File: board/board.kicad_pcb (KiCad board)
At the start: 4 copper layers, 21 x 61 mm, 44 parts, among them J1 UART, J2 008_USB, J3 DebugEdge_02x05, J4 SPI_2x3, J5 ADC_2x3, J6 I2C_2x2, J7 SPI_2x3, J8 I2C_2x2, J9 UART_2x2, U1 W25Q128JVS, U2 RP2040, Y1 12MhZ

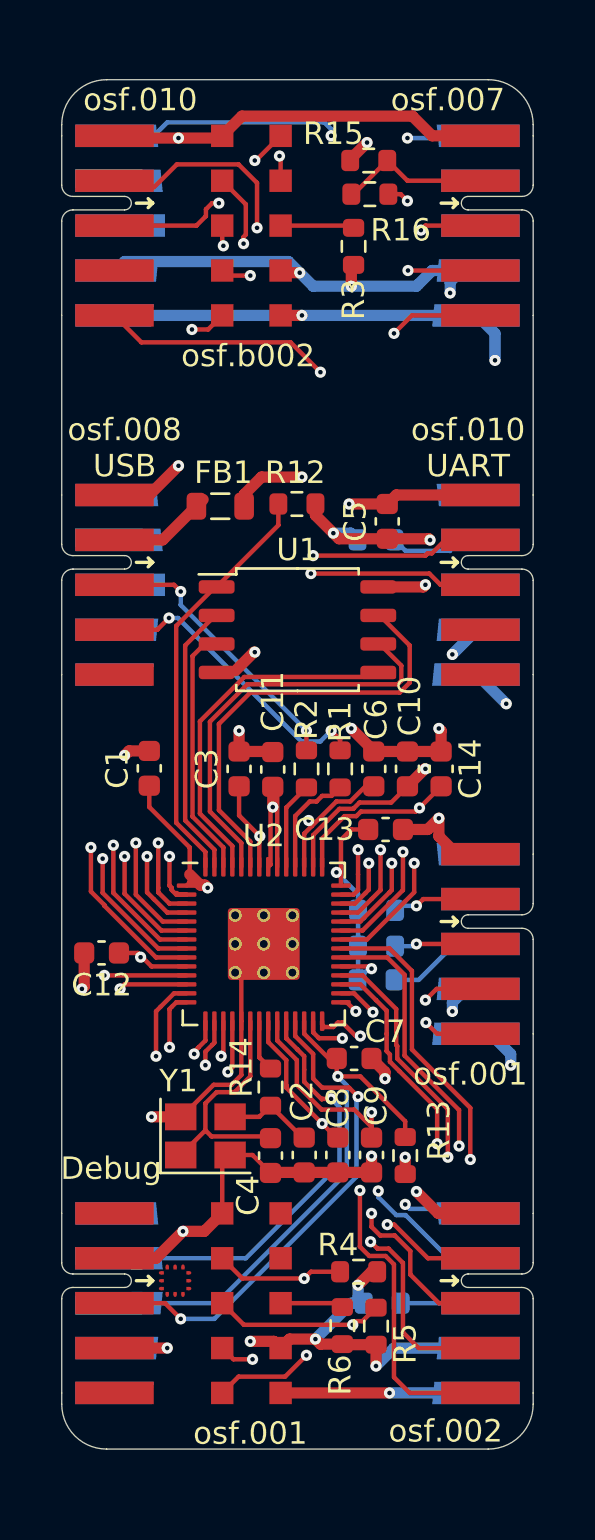
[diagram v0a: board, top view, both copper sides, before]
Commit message: changed top I2C connector to be a UNIO connector for a mac address chip
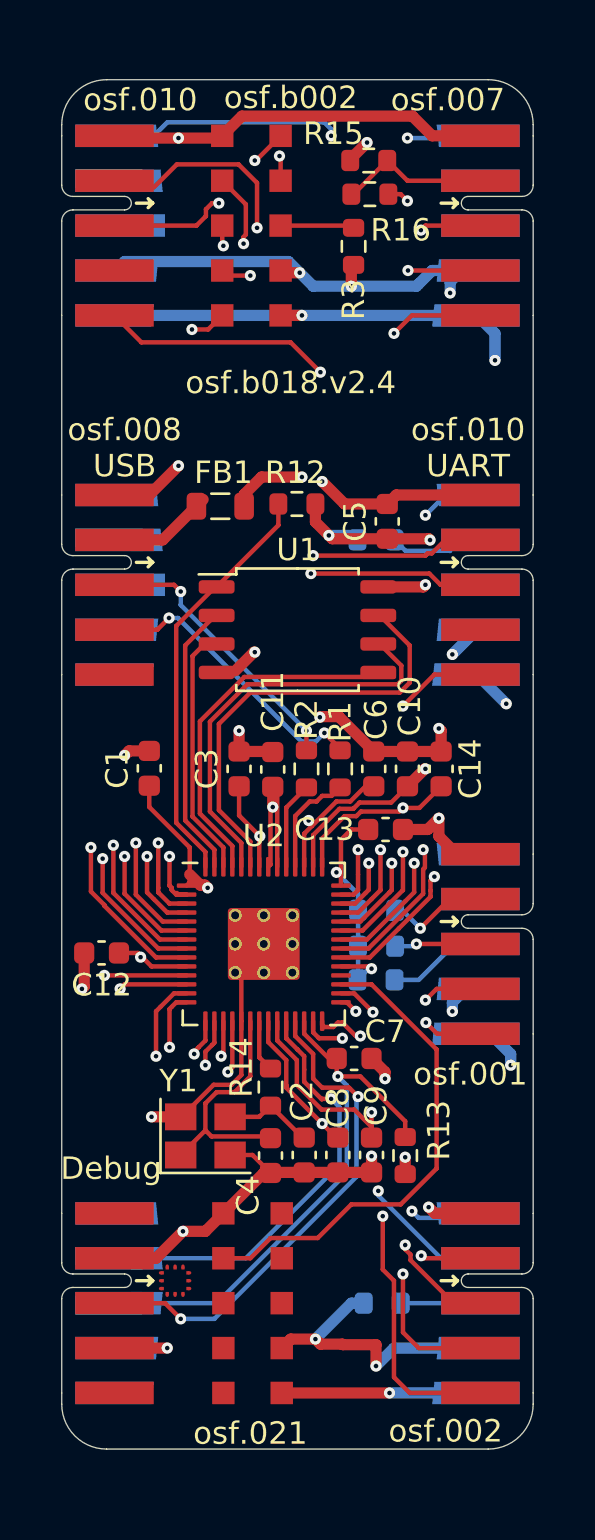
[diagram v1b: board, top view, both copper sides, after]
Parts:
- removed R4, R5: 2k, Resistor_SMD:R_0603_1608Metric
- removed R6: 10k, Resistor_SMD:R_0603_1608Metric
- J6: value I2C_2x2 -> 021_single_IO_UNIO
- moved J6 0.05 mm to (150.8, 96.5)
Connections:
- net /I2C0_SDA renamed /rp2040/GPIO20
- J6 pad 3: /I2C0_SCL -> (no net)
- J6 pad 4: /GPIO23 -> (no net)
- J6 pad 5: /GPIO22 -> (no net)
- J6 pad 8: Net-(J6-Pad8) -> (no net)
- J9 pad 5: unconnected-(J9-Pad5) -> /GPIO23
- J9 pad 6: unconnected-(J9-Pad6) -> /GPIO22
- U2 pad 32: /I2C0_SCL -> /rp2040/GPIO21
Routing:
- net /I2C0_SCL: track 27.4 -> 0.00 mm, vias 2 -> 0
- net /GPIO23: track 30.2 -> 17.8 mm
- net /GPIO22: track 29.2 -> 25.7 mm
- net +3V3: track 199.4 -> 196.4 mm, vias 22 -> 20
- net /rp2040/GPIO20: track 24.7 -> 21.9 mm, vias 2 -> 0
- net Net-(J6-Pad8): track 2.82 -> 0.00 mm
- net GND: track 166.7 -> 167.7 mm
- net /GPIO24: track 42.8 -> 41.9 mm
- net /GPIO25: track 52.5 -> 51.6 mm
- net /~{SPI1_CS}: track 17.4 -> 18.2 mm
- net /SPI1_RX: track 20.7 -> 20.0 mm
- net Net-(C14-Pad1): track 36.8 -> 37.4 mm
- net /GPIO14: track 24.6 -> 24.1 mm
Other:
- board text added: "osf.021"
- board text added: "osf.b018.v2.4"

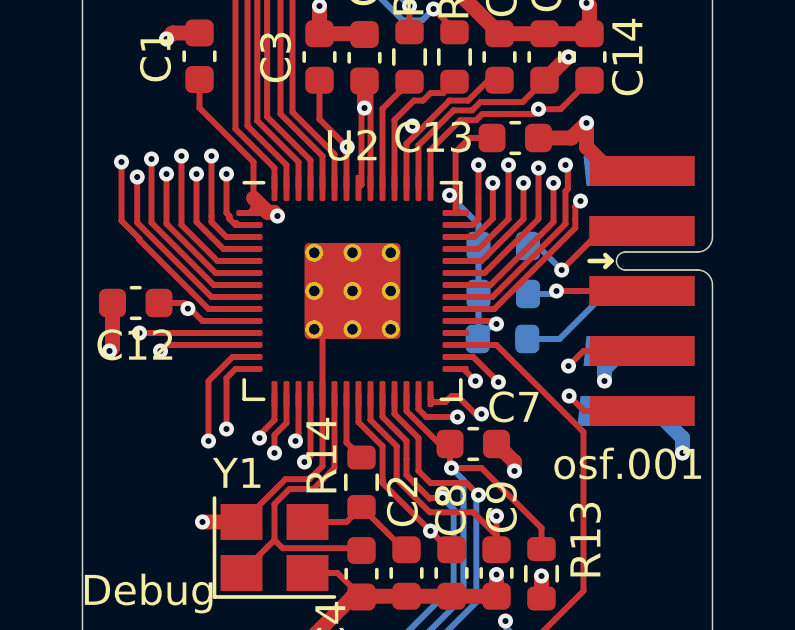
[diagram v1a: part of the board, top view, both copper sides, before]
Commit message: changed power symbols in subsheets
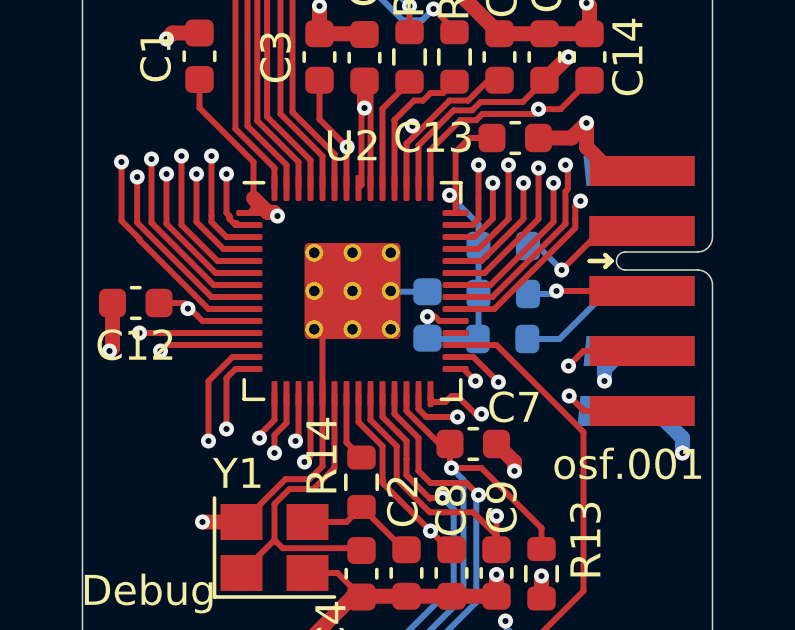
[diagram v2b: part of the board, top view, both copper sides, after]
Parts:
- added C29: 100nF, Capacitor_SMD:C_0603_1608Metric, B.Cu at (151.5, 81.3)
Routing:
- net GND: track 167.7 -> 169.0 mm
- net +3V3: track 196.4 -> 197.6 mm
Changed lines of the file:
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@@
       ) (layer "B.SilkS") (width 0.01) (fill solid))
+  )
+  (footprint "Capacitor_SMD:C_0603_1608Metric" (layer "B.Cu")
+    (at 151.5 81.3 90)
+    (descr "Capacitor SMD 0603 (1608 Metric), square (rectangular) end terminal, IPC_7351 nominal, (Body size source: IPC-SM-782 page 76, https://www.pcb-3d.com/wordpress/wp-content/uploads/ipc-sm-782a_amendment_1_and_2.pdf), generated with kicad-footprint-generator")
+    (tags "capacitor")
+    (property "Sheetfile" "rp2040.kicad_sch")
+    (property "Sheetname" "rp2040")
+    (attr smd)
+    (fp_text reference "C29" (at 0 1.43 90) (layer "B.SilkS")
+      (effects (font (size 1 1) (thickness 0.15)) (justify mirror))
+    )
+    (fp_text value "100nF" (at 0 -1.43 90) (layer "B.Fab")
+      (effects (font (size 1 1) (thickness 0.15)) (justify mirror))
+    )
+    (fp_text user "${REFERENCE}" (at 0 0 90) (layer "B.Fab")
+      (effects (font (size 0.4 0.4) (thickness 0.06)) (justify mirror))
+    )
+    (fp_line (start -0.14058 0.51) (end 0.14058 0.51) (layer "B.SilkS") (width 0.12))
+    (fp_line (start -0.14058 -0.51) (end 0.14058 -0.51) (layer "B.SilkS") (width 0.12))
+    (fp_line (start -1.48 -0.73) (end -1.48 0.73) (layer "B.CrtYd") (width 0.05))
+    (fp_line (start -1.48 0.73) (end 1.48 0.73) (layer "B.CrtYd") (width 0.05))
+    (fp_line (start 1.48 -0.73) (end -1.48 -0.73) (layer "B.CrtYd") (width 0.05))
+    (fp_line (start 1.48 0.73) (end 1.48 -0.73) (layer "B.CrtYd") (width 0.05))
+    (fp_line (start 0.8 0.4) (end 0.8 -0.4) (layer "B.Fab") (width 0.1))
+    (fp_line (start -0.8 0.4) (end 0.8 0.4) (layer "B.Fab") (width 0.1))
+    (fp_line (start -0.8 -0.4) (end -0.8 0.4) (layer "B.Fab") (width 0.1))
+    (fp_line (start 0.8 -0.4) (end -0.8 -0.4) (layer "B.Fab") (width 0.1))
+    (pad "1" smd roundrect (at -0.775 0 90) (size 0.9 0.95) (layers "B.Cu" "B.Paste" "B.Mask") (roundrect_rratio 0.25)
+      (net 1 "+3V3") (pintype "passive"))
+    (pad "2" smd roundrect (at 0.775 0 90) (size 0.9 0.95) (layers "B.Cu" "B.Paste" "B.Mask") (roundrect_rratio 0.25)
+      (net 2 "GND") (pintype "passive"))
+    (model "${KICAD6_3DMODEL_DIR}/Capacitor_SMD.3dshapes/C_0603_1608Metric.wrl"
+      (offset (xyz 0 0 0))
+      (scale (xyz 1 1 1))
+      (rotate (xyz 0 0 0))
+    )
   )
   (footprint "Resistor_SMD:R_0603_1608Metric" (layer "B.Cu")
@@
   (segment (start 150 86.9) (end 151.6 88.5) (width 0.2) (layer "F.Cu") (net 1))
   (segment (start 145.5625 81.5) (end 144 81.5) (width 0.2) (layer "F.Cu") (net 1))
+  (segment (start 151.9 81.5) (end 152.4375 81.5) (width 0.2) (layer "F.Cu") (net 1))
   (segment (start 149.2 77.0625) (end 149.3 76.9625) (width 0.2) (layer "F.Cu") (net 1))
   (segment (start 152.4375 77.9) (end 152.4375 77.2625) (width 0.2) (layer "F.Cu") (net 1))
@@
   (segment (start 152.225 89.125) (end 151.6 88.5) (width 0.2) (layer "F.Cu") (net 1))
   (segment (start 156.105 64.595) (end 156.2 64.5) (width 0.5) (layer "F.Cu") (net 1))
+  (segment (start 151.7515 81.3515) (end 151.9 81.5) (width 0.2) (layer "F.Cu") (net 1))
   (segment (start 149.4 74.4) (end 149.4 73.5) (width 0.5) (layer "F.Cu") (net 1))
   (segment (start 152.525 98.35) (end 152.5 98.325) (width 0.5) (layer "F.Cu") (net 1))
   (segment (start 151.2 77.0625) (end 151.2 75.649896) (width 0.2) (layer "F.Cu") (net 1))
+  (segment (start 151.5 81.3515) (end 151.7515 81.3515) (width 0.2) (layer "F.Cu") (net 1))
   (segment (start 149.3 73.6) (end 149.4 73.5) (width 0.2) (layer "F.Cu") (net 1))
   (segment (start 152.235779 77.309653) (end 152.282932 77.2625) (width 0.2) (layer "F.Cu") (net 1))
@@
   (segment (start 144 81.5) (end 143.4 80.9) (width 0.2) (layer "F.Cu") (net 1))
   (segment (start 143.4 80.9) (end 142.55 80.9) (width 0.2) (layer "F.Cu") (net 1))
-  (segment (start 153.7 81.5) (end 153.8 81.6) (width 0.2) (layer "F.Cu") (net 1))
   (segment (start 149.85 50.6) (end 149.75 50.5) (width 0.5) (layer "F.Cu") (net 1))
   (segment (start 151.3 98.1) (end 150.2 98.1) (width 0.5) (layer "F.Cu") (net 1))
@@
   (segment (start 152.4375 75.8625) (end 152.9 75.4) (width 0.2) (layer "F.Cu") (net 1))
   (segment (start 154 99.3) (end 154 98.35) (width 0.5) (layer "F.Cu") (net 1))
-  (segment (start 152.4375 81.5) (end 153.7 81.5) (width 0.2) (layer "F.Cu") (net 1))
   (via (at 149.4 74.4) (size 0.5) (drill 0.2) (layers "F.Cu" "B.Cu") (net 1))
   (via (at 152.235779 77.309653) (size 0.5) (drill 0.2) (layers "F.Cu" "B.Cu") (net 1))
@@
   (via (at 157.4 83.5) (size 0.5) (drill 0.2) (layers "F.Cu" "B.Cu") (net 1))
   (via (at 150.6 50.6) (size 0.5) (drill 0.2) (layers "F.Cu" "B.Cu") (net 1))
+  (via (at 151.5 81.3515) (size 0.5) (drill 0.2) (layers "F.Cu" "B.Cu") (net 1))
   (via (at 156.406644 62.506644) (size 0.5) (drill 0.2) (layers "F.Cu" "B.Cu") (net 1))
   (via (at 151.9 62.3) (size 0.5) (drill 0.2) (layers "F.Cu" "B.Cu") (net 1))
-  (via (at 153.8 81.6) (size 0.5) (drill 0.2) (layers "F.Cu" "B.Cu") (net 1))
   (via (at 154 99.3) (size 0.5) (drill 0.2) (layers "F.Cu" "B.Cu") (net 1))
   (via (at 152.9 51.2) (size 0.5) (drill 0.2) (layers "F.Cu" "B.Cu") (net 1))
@@
   (segment (start 153.2 78.273874) (end 152.235779 77.309653) (width 0.2) (layer "B.Cu") (net 1))
   (segment (start 157.4 83.1) (end 158 82.5) (width 0.5) (layer "B.Cu") (net 1))
+  (segment (start 153.175 82.1) (end 151.525 82.1) (width 0.2) (layer "B.Cu") (net 1))
   (segment (start 157.4 83.5) (end 157.4 83.1) (width 0.5) (layer "B.Cu") (net 1))
   (segment (start 153.2 79) (end 153.2 78.273874) (width 0.2) (layer "B.Cu") (net 1))
+  (segment (start 151.5 82.075) (end 151.5 81.3515) (width 0.2) (layer "B.Cu") (net 1))
   (segment (start 150.1 50.1) (end 142.8 50.1) (width 0.5) (layer "B.Cu") (net 1))
   (segment (start 151.2 51.2) (end 150.6 50.6) (width 0.5) (layer "B.Cu") (net 1))
+  (segment (start 151.525 82.1) (end 151.5 82.075) (width 0.2) (layer "B.Cu") (net 1))
   (segment (start 152.9 96.5) (end 151.3 98.1) (width 0.5) (layer "B.Cu") (net 1))
   (segment (start 153.45 96.5) (end 152.9 96.5) (width 0.5) (layer "B.Cu") (net 1))
@@
   (segment (start 152.9 51.2) (end 151.2 51.2) (width 0.5) (layer "B.Cu") (net 1))
   (segment (start 157.4 67.6) (end 158.5 66.5) (width 0.5) (layer "B.Cu") (net 1))
-  (segment (start 153.675 81.6) (end 153.175 82.1) (width 0.2) (layer "B.Cu") (net 1))
   (segment (start 158 82.5) (end 158.6 82.5) (width 0.5) (layer "B.Cu") (net 1))
   (segment (start 142.8 50.1) (end 142.4 50.5) (width 0.5) (layer "B.Cu") (net 1))
-  (segment (start 153.8 81.6) (end 153.675 81.6) (width 0.2) (layer "B.Cu") (net 1))
   (segment (start 154.8 98.5) (end 154 99.3) (width 0.5) (layer "B.Cu") (net 1))
   (segment (start 154.4 86.2) (end 153.8 85.6) (width 0.5) (layer "F.Cu") (net 2))
@@
   (segment (start 148.527 70.373) (end 147.9 71) (width 0.5) (layer "In2.Cu") (net 2))
   (segment (start 145.2 59.2) (end 148.6 62.6) (width 0.5) (layer "In2.Cu") (net 2))
+  (segment (start 150.3 80.525) (end 150.275 80.5) (width 0.2) (layer "B.Cu") (net 2))
+  (segment (start 151.5 80.525) (end 150.3 80.525) (width 0.2) (layer "B.Cu") (net 2))
   (segment (start 150.725 89.125) (end 149.3 87.7) (width 0.2) (layer "F.Cu") (net 3))
   (segment (start 147.5 88.2) (end 148.8 88.2) (width 0.2) (layer "F.Cu") (net 3))

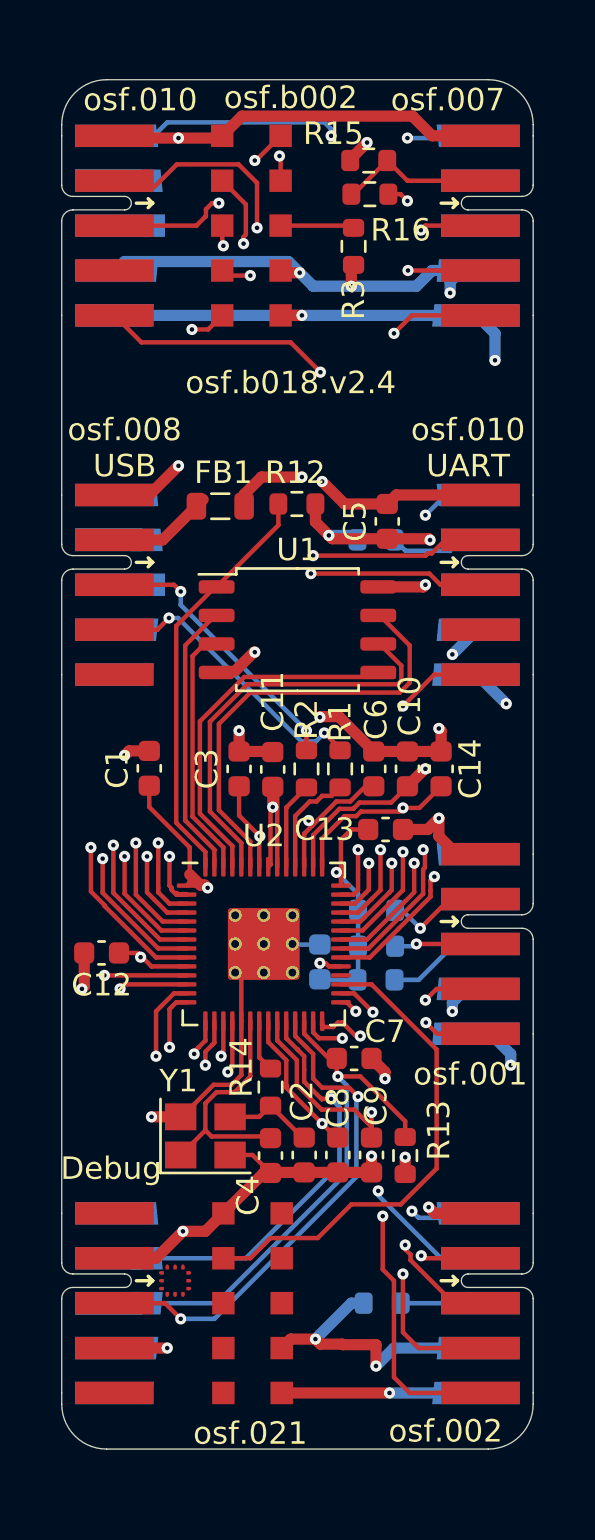
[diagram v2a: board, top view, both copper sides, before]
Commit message: updated connector footprints and added planes
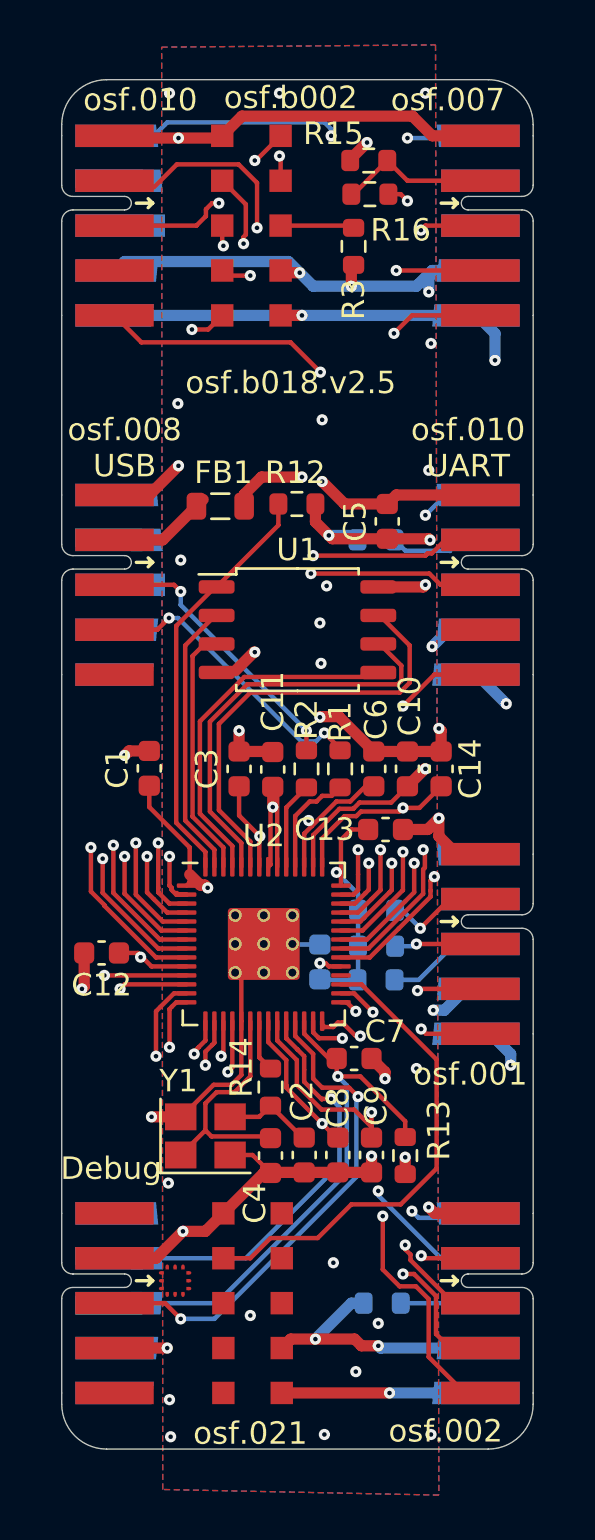
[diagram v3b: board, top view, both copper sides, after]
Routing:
- net /GPIO14: track 24.1 -> 23.0 mm
- net +3V3: track 197.6 -> 198.4 mm
- net /ADC1: track 33.9 -> 34.5 mm
- net /SPI1_SCK: track 25.3 -> 24.8 mm
- net GND: vias 15 -> 36
- added copper zone on B.Cu, net GND
- added copper zone on F.Cu, net GND
- added copper zone on In2.Cu, net GND
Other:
- board text added: "osf.b018.v2.5"
- board text removed: "osf.b018.v2.4"

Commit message: upgraded to new kicad and switched to standard flash
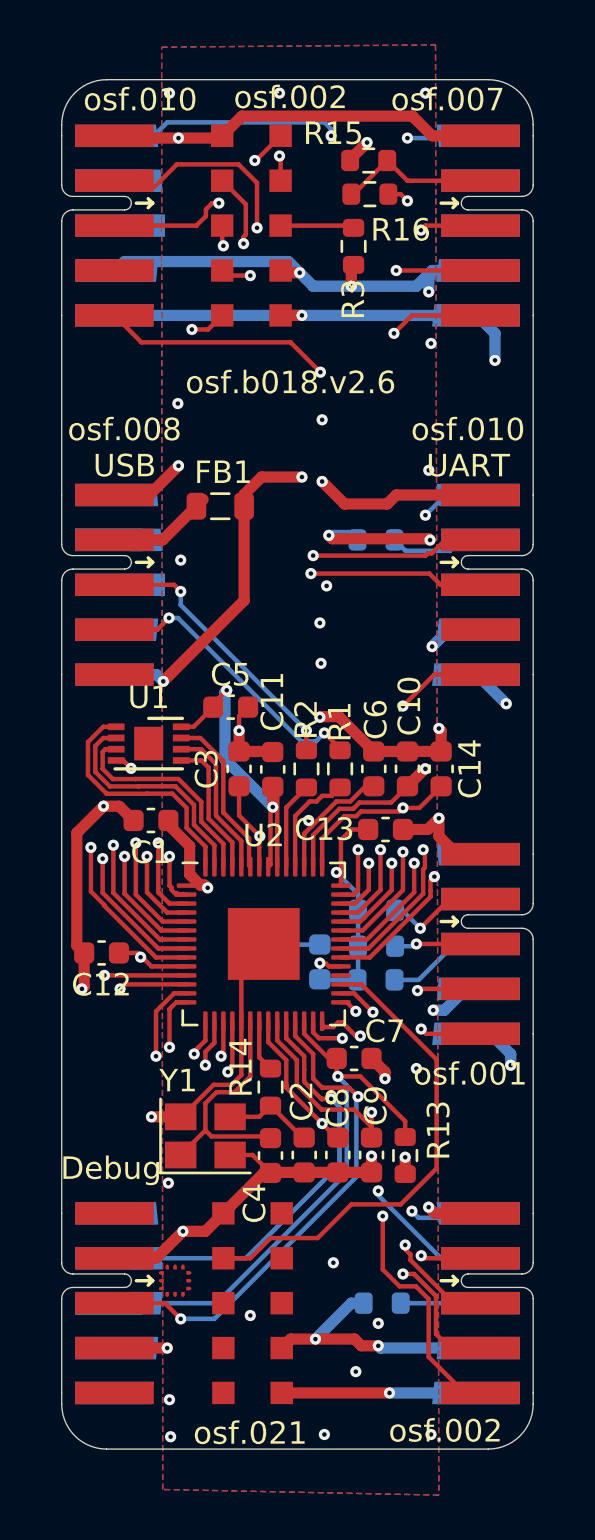
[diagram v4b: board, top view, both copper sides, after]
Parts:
- removed R12: d.n.p, Resistor_SMD:R_0603_1608Metric
- U1: value W25Q128JVS -> W25Q16JVUXIQ; footprint Package_SO:SOIC-8_5.23x5.23mm_P1.27mm -> Package_DFN_QFN:DFN-8-1EP_3x2mm_P0.5mm_EP1.3x1.5mm
- U2: footprint b018:RP2040-QFN-56 -> Package_DFN_QFN:QFN-56-1EP_7x7mm_P0.4mm_EP3.2x3.2mm
- moved C5 10.8 mm to (147.5, 70.0), turned to 0 degrees
- moved U1 8.35 mm to (143.9, 71.6)
- moved C1 2.33 mm to (144.0, 75.0), turned to 180 degrees
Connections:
- net +3V3 renamed +3.3V
- J2 pad 10: (no net) -> +5V
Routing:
- net Net-(U1-IO3): track 19.8 -> 7.51 mm
- net +5V: track 95.8 -> 107.4 mm, vias 6 -> 7
- net /rp2040/QSPI_CLK: track 18.4 -> 6.87 mm
- net GND: track 169.0 -> 180.0 mm
- net Net-(U1-DI(IO0)): track 16.5 -> 6.21 mm
- net /rp2040/QPI_SS: track 18.6 -> 11.0 mm
- net Net-(U1-DO(IO1)): track 12.4 -> 10.4 mm
- net +3.3V: track 198.4 -> 200.4 mm
- net Net-(U1-IO2): track 11.3 -> 9.71 mm
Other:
- board text added: "osf.b018.v2.6"
- board text removed: "osf.b002"
- board text removed: "osf.b018.v2.5"
